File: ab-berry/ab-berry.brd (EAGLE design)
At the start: 58.4 x 61 mm, 40 parts, among them U1 LM1117MPX-3.3/NOPB or AP2114H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

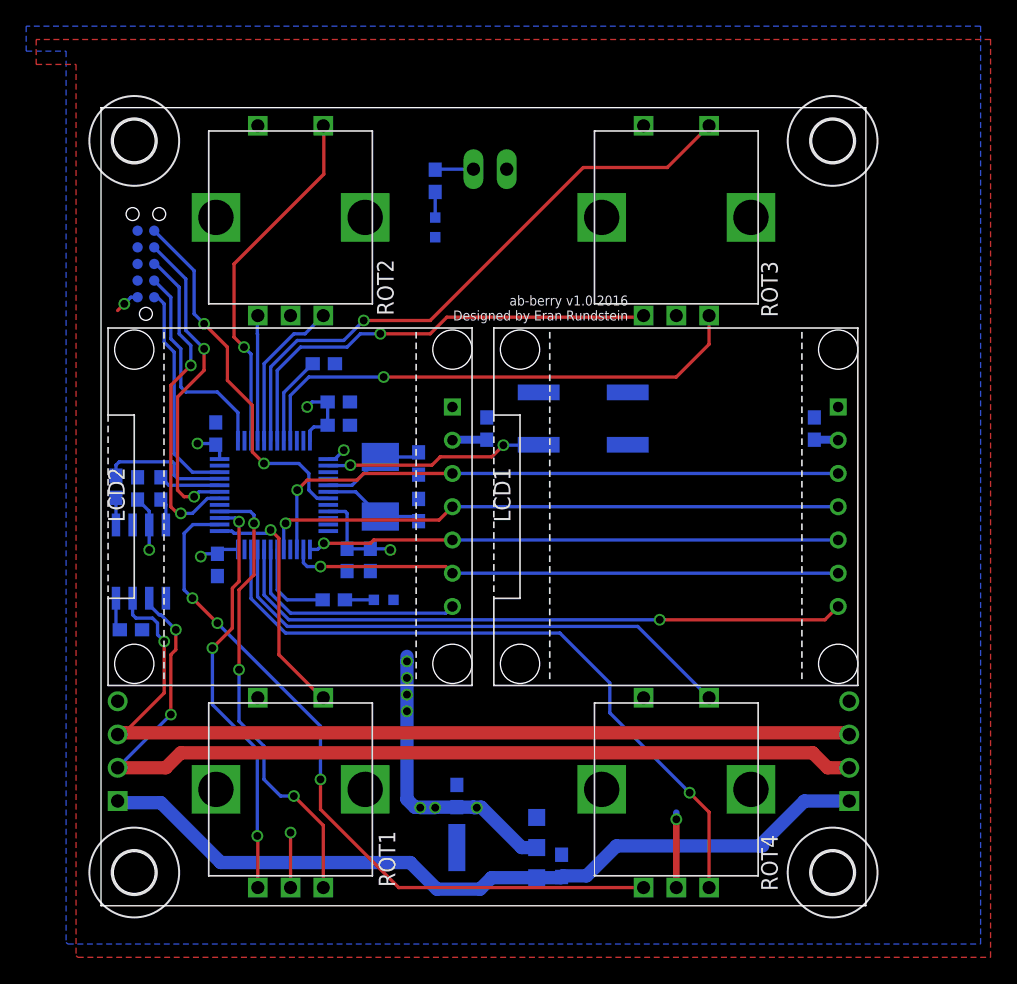
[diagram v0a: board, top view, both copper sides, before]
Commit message: ab-berry: add rc filter network to rotencs
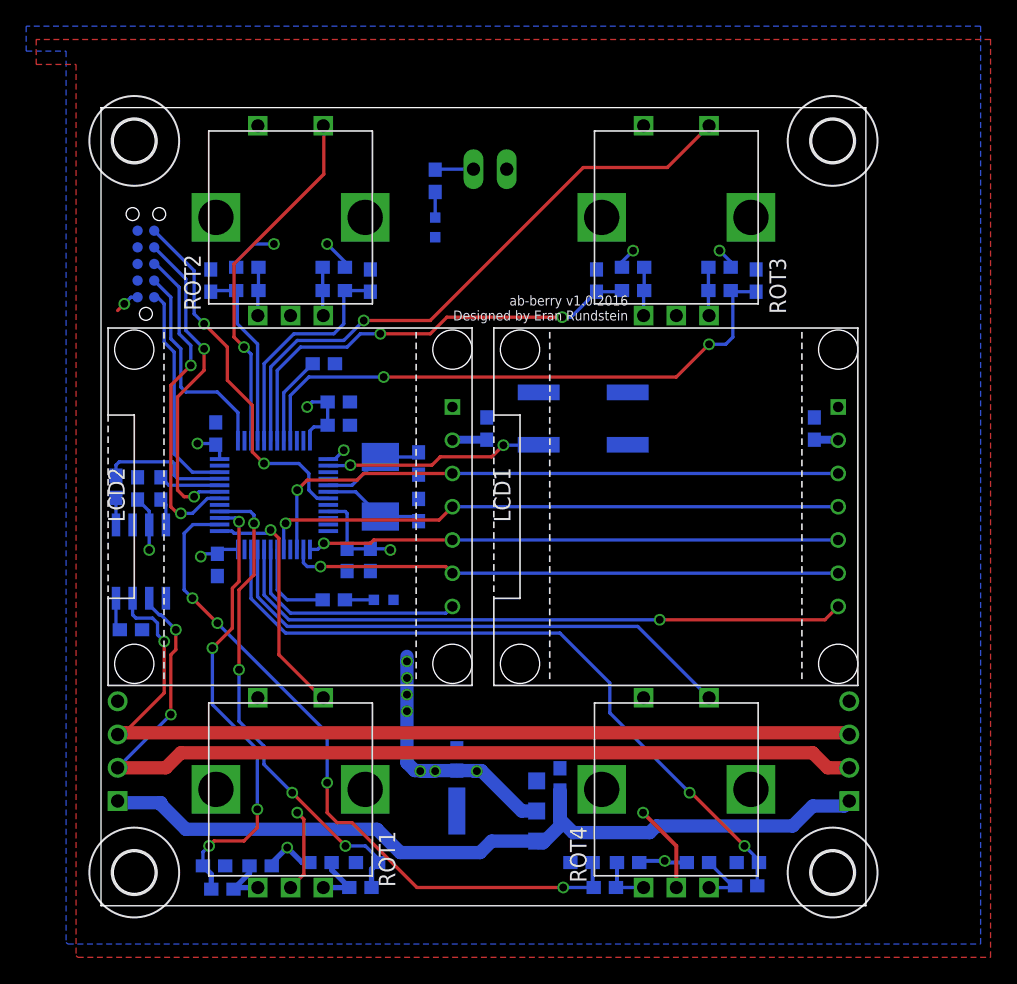
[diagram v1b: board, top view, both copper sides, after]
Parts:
- added C14, C15, C16, C17, C18, C19, C20, C21: 0.01uF, microbuilder:0603
- added R10, R11, R12, R13, R14, R15, R16, R17, R18, R19, R20, R21, R22, R7, R8, R9: 10K, microbuilder:0603
- moved C8 6.61 mm to (35.1, 9.65)
- moved C9 2.79 mm to (27.2, 11.2)
- moved U1 2.79 mm to (30.2, 7.24)
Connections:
- new net N$10: R10.2, R8.2, ROT1.B
- new net N$11: R7.2, R9.2, ROT1.A
- new net N$12: R12.2, R14.2, ROT4.B
- new net N$13: R11.2, R13.2, ROT4.A
- new net N$14: R16.2, R18.2, ROT2.B
- new net N$15: R15.2, R17.2, ROT2.A
- new net N$16: R20.2, R22.2, ROT3.B
- new net N$17: R19.2, R21.2, ROT3.A
- net 3.3V: now also R10.1, R13.1, R14.1, R17.1, R18.1, R21.1, R22.1, R9.1
- net GND: now also C14.2, C15.2, C16.2, C17.2, C18.2, C19.2, C20.2, C21.2
- net ROT1_A: now also C14.1, R7.1; no longer ROT1.A
- net ROT1_B: now also C15.1, R8.1; no longer ROT1.B
- net ROT2_A: now also C18.1, R15.1; no longer ROT2.A
- net ROT2_B: now also C19.1, R16.1; no longer ROT2.B
- net ROT3_A: now also C20.1, R19.1; no longer ROT3.A
- net ROT3_B: now also C21.1, R20.1; no longer ROT3.B
- net ROT4_A: now also C16.1, R11.1; no longer ROT4.A
- net ROT4_B: now also C17.1, R12.1; no longer ROT4.B
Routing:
- net 3.3V: track 59.3 -> 75.6 mm, vias 14 -> 20
- net ROT2_B: track 11.9 -> 17.8 mm
- net ROT3_B: track 39.2 -> 44.7 mm, vias 1 -> 2
- net N$12: track 0.00 -> 4.55 mm
- net ROT2_A: track 9.58 -> 14.1 mm
- net N$10: track 0.00 -> 4.45 mm
- net N$11: track 0.00 -> 4.26 mm
- net N$13: track 0.00 -> 4.05 mm
- net N$16: track 0.00 -> 3.71 mm
- net N$14: track 0.00 -> 3.71 mm
- net N$17: track 0.00 -> 3.71 mm
- net N$15: track 0.00 -> 3.71 mm
- net ROT1_A: track 31.8 -> 35.3 mm, vias 3 -> 4
- net GND: track 9.92 -> 13.1 mm
- net 5.0V: track 61.7 -> 64.8 mm
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
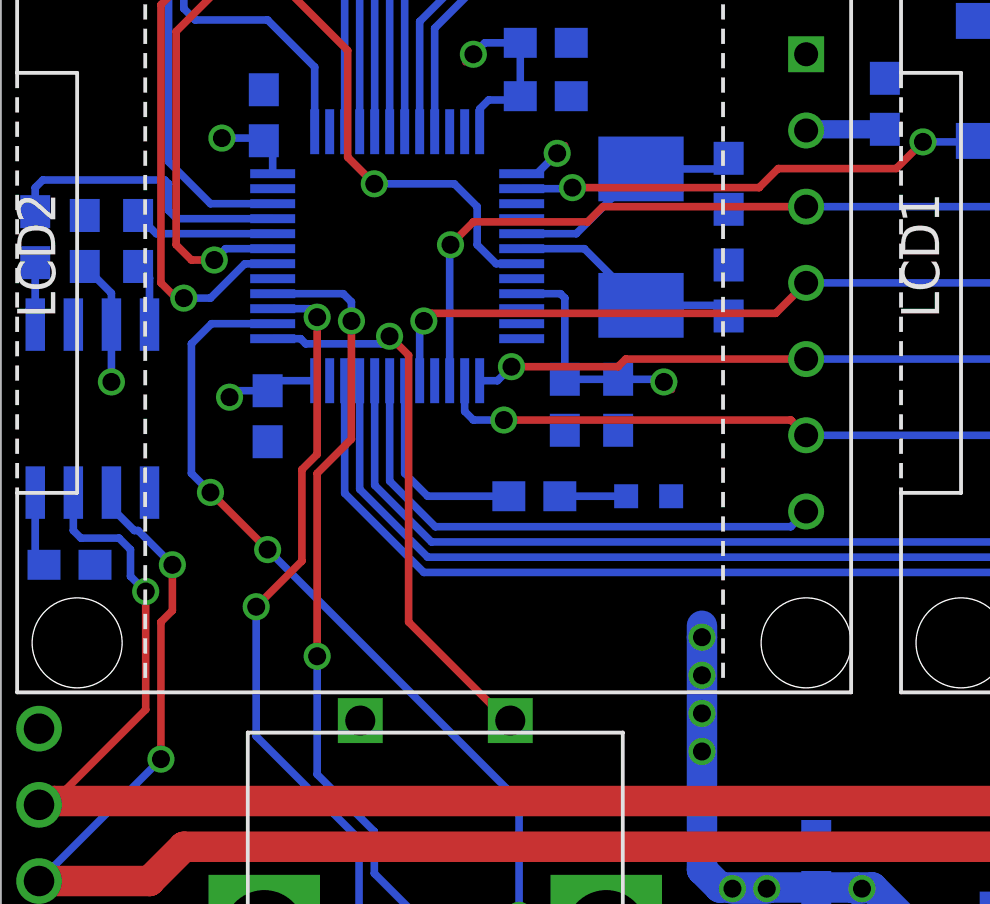
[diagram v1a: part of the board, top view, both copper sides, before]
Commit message: ab-berry: small layout cleanup
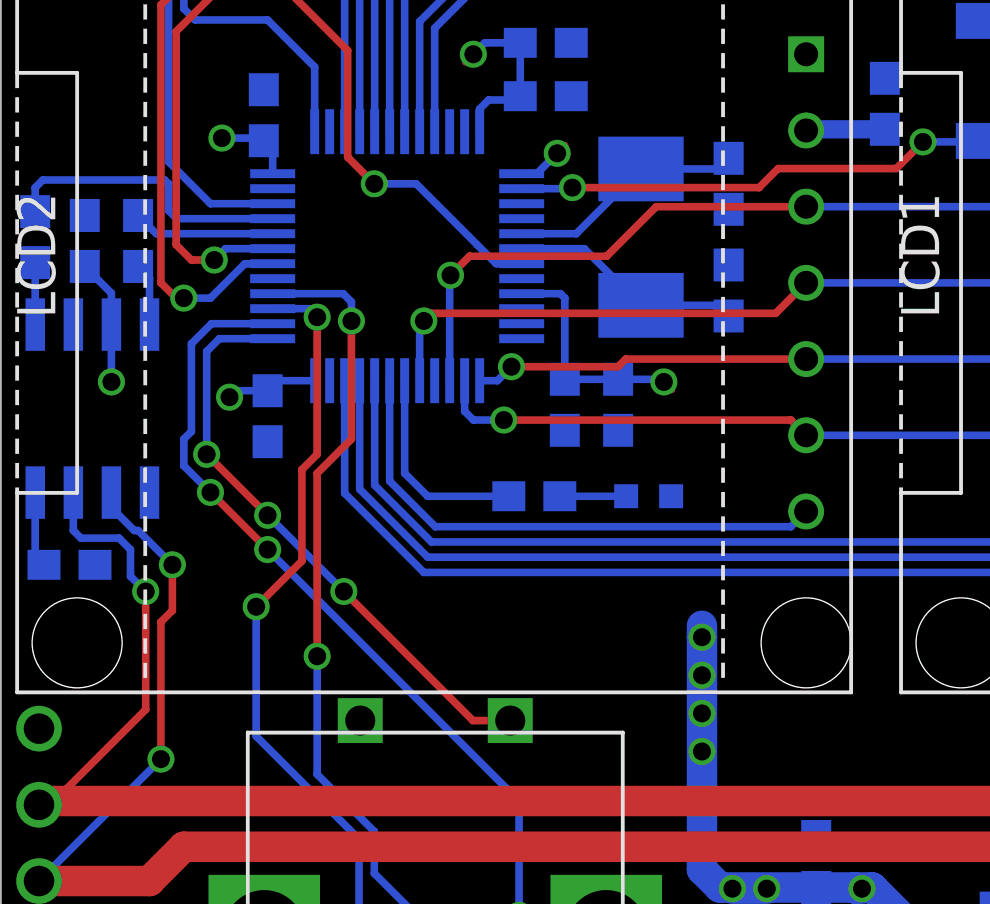
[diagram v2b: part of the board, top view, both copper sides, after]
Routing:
- net ROT1_SW: track 18.6 -> 19.6 mm, vias 1 -> 3
- net RST: track 28.0 -> 27.3 mm
- net SPI1_CLK: track 46.4 -> 45.8 mm
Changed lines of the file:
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@@
 <setting verticaltext="up"/>
 </settings>
-<grid distance="10" unitdist="mil" unit="mm" style="lines" multiple="1" display="no" altdistance="0.025" altunitdist="inch" altunit="inch"/>
+<grid distance="5" unitdist="mil" unit="mil" style="lines" multiple="1" display="no" altdistance="0.025" altunitdist="inch" altunit="inch"/>
 <layers>
 <layer number="1" name="Top" color="4" fill="1" visible="yes" active="yes"/>
@@
 <wire x1="7.112" y1="45.212" x2="7.874" y2="44.45" width="0.254" layer="16"/>
 <wire x1="17.358" y1="31.119" x2="16.506" y2="31.119" width="0.254" layer="16"/>
-<wire x1="16.506" y1="31.119" x2="15.875" y2="31.75" width="0.254" layer="16"/>
-<wire x1="15.875" y1="31.75" x2="15.875" y2="33.02" width="0.254" layer="16"/>
-<wire x1="15.875" y1="33.02" x2="15.113" y2="33.782" width="0.254" layer="16"/>
-<wire x1="15.113" y1="33.782" x2="12.446" y2="33.782" width="0.254" layer="16"/>
+<wire x1="16.506" y1="31.119" x2="16.256" y2="31.369" width="0.254" layer="16"/>
+<wire x1="16.256" y1="31.369" x2="15.875" y2="31.75" width="0.254" layer="16"/>
 <via x="12.446" y="33.782" extent="1-16" drill="0.6"/>
 <wire x1="12.446" y1="33.782" x2="11.557" y2="34.671" width="0.254" layer="1"/>
@@
 <wire x1="11.557" y1="38.227" x2="9.652" y2="40.132" width="0.254" layer="1"/>
 <wire x1="9.652" y1="40.132" x2="9.652" y2="42.672" width="0.254" layer="1"/>
+<wire x1="12.446" y1="33.782" x2="13.843" y2="33.782" width="0.254" layer="16"/>
+<wire x1="13.843" y1="33.782" x2="15.875" y2="31.75" width="0.254" layer="16"/>
 </signal>
 <signal name="DBG_TX">
@@
 <contactref element="ROT1" pad="S2"/>
 <contactref element="STM32F072CBT6" pad="25"/>
-<wire x1="16.978" y1="15.89" x2="16.876" y2="15.89" width="0.254" layer="1"/>
-<wire x1="16.876" y1="15.89" x2="13.589" y2="19.177" width="0.254" layer="1"/>
-<wire x1="13.589" y1="19.177" x2="13.589" y2="28.067" width="0.254" layer="1"/>
-<wire x1="9.058" y1="28.619" x2="9.989" y2="28.619" width="0.254" layer="16"/>
-<wire x1="9.989" y1="28.619" x2="10.16" y2="28.448" width="0.254" layer="16"/>
-<via x="12.954" y="28.702" extent="1-16" drill="0.6"/>
-<wire x1="10.16" y1="28.448" x2="12.7" y2="28.448" width="0.254" layer="16"/>
-<wire x1="12.7" y1="28.448" x2="12.954" y2="28.702" width="0.254" layer="16"/>
-<wire x1="13.589" y1="28.067" x2="12.954" y2="28.702" width="0.254" layer="1"/>
+<wire x1="9.058" y1="28.619" x2="7.283" y2="28.619" width="0.254" layer="16"/>
+<wire x1="7.283" y1="28.619" x2="6.858" y2="28.194" width="0.254" layer="16"/>
+<wire x1="6.858" y1="28.194" x2="6.858" y2="24.765" width="0.254" layer="16"/>
+<via x="11.43" y="20.193" extent="1-16" drill="0.6"/>
+<wire x1="16.978" y1="15.89" x2="15.733" y2="15.89" width="0.254" layer="1"/>
+<wire x1="15.733" y1="15.89" x2="11.43" y2="20.193" width="0.254" layer="1"/>
+<via x="6.858" y="24.765" extent="1-16" drill="0.6"/>
+<wire x1="6.858" y1="24.765" x2="8.89" y2="22.733" width="0.254" layer="1"/>
+<via x="8.89" y="22.733" extent="1-16" drill="0.6"/>
+<wire x1="8.89" y1="22.733" x2="11.43" y2="20.193" width="0.254" layer="16"/>
 </signal>
 <signal name="ROT2_A">
@@
 <via x="6.985" y="23.495" extent="1-16" drill="0.6"/>
 <wire x1="6.985" y1="23.495" x2="8.89" y2="21.59" width="0.254" layer="1"/>
-<wire x1="6.35" y1="28.448" x2="6.35" y2="24.13" width="0.254" layer="16"/>
-<wire x1="6.35" y1="24.13" x2="6.985" y2="23.495" width="0.254" layer="16"/>
+<wire x1="6.096" y1="24.384" x2="6.985" y2="23.495" width="0.254" layer="16"/>
 <via x="8.89" y="21.59" extent="1-16" drill="0.6"/>
 <wire x1="19.177" y1="6.35" x2="18.034" y2="6.35" width="0.254" layer="1"/>
@@
 <wire x1="37.553" y1="3.302" x2="37.553" y2="1.475" width="0.3048" layer="16"/>
 <wire x1="37.553" y1="1.475" x2="37.631" y2="1.397" width="0.3048" layer="16"/>
+<wire x1="6.35" y1="28.448" x2="6.35" y2="25.527" width="0.254" layer="16"/>
+<wire x1="6.35" y1="25.527" x2="6.096" y2="25.273" width="0.254" layer="16"/>
+<wire x1="6.096" y1="25.273" x2="6.096" y2="24.384" width="0.254" layer="16"/>
 </signal>
 <signal name="ROT4_B">
@@
 <contactref element="STM32F072CBT6" pad="15"/>
 <wire x1="56.304" y1="33.02" x2="26.84" y2="33.02" width="0.254" layer="16"/>
-<via x="14.986" y="31.75" extent="1-16" drill="0.6"/>
-<wire x1="14.958" y1="27.219" x2="14.958" y2="31.722" width="0.254" layer="16"/>
-<wire x1="26.84" y1="33.02" x2="20.066" y2="33.02" width="0.254" layer="1"/>
-<wire x1="20.066" y1="33.02" x2="19.558" y2="32.512" width="0.254" layer="1"/>
-<wire x1="19.558" y1="32.512" x2="15.748" y2="32.512" width="0.254" layer="1"/>
-<wire x1="15.748" y1="32.512" x2="14.986" y2="31.75" width="0.254" layer="1"/>
-<wire x1="14.958" y1="31.722" x2="14.986" y2="31.75" width="0.254" layer="16"/>
+<via x="14.986" y="30.734" extent="1-16" drill="0.6"/>
+<wire x1="14.958" y1="27.219" x2="14.958" y2="30.706" width="0.254" layer="16"/>
+<wire x1="14.958" y1="30.706" x2="14.986" y2="30.734" width="0.254" layer="16"/>
+<wire x1="26.84" y1="33.02" x2="21.844" y2="33.02" width="0.254" layer="1"/>
+<wire x1="21.844" y1="33.02" x2="20.193" y2="31.369" width="0.254" layer="1"/>
+<wire x1="20.193" y1="31.369" x2="15.621" y2="31.369" width="0.254" layer="1"/>
+<wire x1="15.621" y1="31.369" x2="14.986" y2="30.734" width="0.254" layer="1"/>
 </signal>
 <signal name="LCD_CS2">
